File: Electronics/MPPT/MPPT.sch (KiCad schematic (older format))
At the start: 24 parts, among them J1 Solar Array, J2 Battery, J3 Car Power, Q1 NMOS, Q2 NMOS

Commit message: MPPT: Add power lines and regulators
There are three primary power regions on the board: the high power regions around the DC/DC Converter, the car's "low" power regions (+12V), and the low power regions around the Nucleo.

The high power regions include current sensors and FET drivers which require power from the car's low power line rather than the high power lines from the solar array and the battery. We use a 12V-12V DC isolator to provide this safely.

We also isolate power to the Nucleo for safety when attaching a computer to the board. Finally, the CAN lines have an isolated power region, but this is managed by the CAN chip.
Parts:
- added U?: Nucleo_L432KC, symbol Nucleo_L432KC
- added U?: PDS1-S12-S9-M, symbol PDS1-S12-S9-M
- added U?: PDM2-S12-S12-S, symbol PDM2-S12-S12-S
- C3: value CP1 -> CP
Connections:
- net labels added: +12V, +5V, +9V, GND
- wire segments 94 -> 86
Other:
- note added: "High Power\nControl"
- note added: "Isolated Power Regions:\n* High Power\n - Arr+\n - Batt+\n - +12P\n - GNDPWR\n* Low Car Power\n - +12V\n - GNDREF\n* Nucleo/Computer Power\n - +9V\n - +5V\n - GND"
- note added: "Note: Current sensors may be\non ground line, not high line"
- note added: "Nucleo Power"
- note added: "Power Regulation"
- note removed: "Power and Isolation"
- moved on the sheet: J3

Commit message: MPPT: Add FET driver and its Nucleo connection
The FET driver doesn't provide any isolation, and it needs to be on the High Power plane, so we will need to add isolation on its PWM input to protect the Nucleo.

We should also figure out whether tying the chip's Enable pin to the PWM input is appropriate or not. According to the datasheet, the enable pin is internally pulled up to Vdd by a 100Kohm resistor, so it may draw unexpected current from the PWM line.
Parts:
- added R?: 1R5, symbol R
- added U?: UCC27321, symbol UCC27321
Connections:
- wire segments 86 -> 99
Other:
- note added: "TODO: Add isolation here.\nEither a new chip or an isolating\nchip on the Nucleo side."
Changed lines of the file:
@@
 LIBS:utsvt-power-regulators
 LIBS:utsvt-microcontrollers
+LIBS:utsvt-connectors
+LIBS:utsvt-chips
 LIBS:MPPT-cache
 EELAYER 25 0
@@
 Wire Notes Line
 	10400 650  7750 650
+Wire Wire Line
+	6300 4900 7100 4900
+$Comp
+L UCC27321 U?
+U 1 1 5BBC0485
+P 7600 4950
+F 0 "U?" H 7600 4700 60  0000 C CNN
+F 1 "UCC27321" H 7600 5200 60  0000 C CNN
+F 2 "" H 7600 4950 60  0001 C CNN
+F 3 "" H 7600 4950 60  0001 C CNN
+	1    7600 4950
+	1    0    0    -1
+$EndComp
+$Comp
+L R R?
+U 1 1 5BBC08B0
+P 8450 4900
+F 0 "R?" V 8530 4900 50  0000 C CNN
+F 1 "1R5" V 8450 4900 50  0000 C CNN
+F 2 "" V 8380 4900 50  0001 C CNN
+F 3 "" H 8450 4900 50  0001 C CNN
+	1    8450 4900
+	0    1    1    0
+$EndComp
+Wire Wire Line
+	8100 4900 8300 4900
+Wire Wire Line
+	8100 5000 8200 5000
+Wire Wire Line
+	8200 5000 8200 4900
+Connection ~ 8200 4900
+Wire Wire Line
+	8600 4900 8700 4900
+Text Label 8700 4900 0    60   ~ 12
+Drive_PWM
+$Comp
+L +12P #PWR?
+U 1 1 5BBC0ED7
+P 8150 4750
+F 0 "#PWR?" H 8150 4600 50  0001 C CNN
+F 1 "+12P" H 8150 4890 50  0000 C CNN
+F 2 "" H 8150 4750 50  0001 C CNN
+F 3 "" H 8150 4750 50  0001 C CNN
+	1    8150 4750
+	1    0    0    -1
+$EndComp
+$Comp
+L GNDPWR #PWR?
+U 1 1 5BBC0FAD
+P 8150 5150
+F 0 "#PWR?" H 8150 4950 50  0001 C CNN
+F 1 "GNDPWR" H 8150 5020 50  0000 C CNN
+F 2 "" H 8150 5100 50  0001 C CNN
+F 3 "" H 8150 5100 50  0001 C CNN
+	1    8150 5150
+	1    0    0    -1
+$EndComp
+Wire Wire Line
+	8100 5100 8150 5100
+Wire Wire Line
+	8150 5100 8150 5150
+Wire Wire Line
+	8100 4800 8150 4800
+Wire Wire Line
+	8150 4800 8150 4750
+$Comp
+L +12P #PWR?
+U 1 1 5BBC1539
+P 7050 4750
+F 0 "#PWR?" H 7050 4600 50  0001 C CNN
+F 1 "+12P" H 7050 4890 50  0000 C CNN
+F 2 "" H 7050 4750 50  0001 C CNN
+F 3 "" H 7050 4750 50  0001 C CNN
+	1    7050 4750
+	1    0    0    -1
+$EndComp
+Wire Wire Line
+	7050 4750 7050 4800
+Wire Wire Line
+	7050 4800 7100 4800
+$Comp
+L GNDPWR #PWR?
+U 1 1 5BBC165F
+P 7050 5150
+F 0 "#PWR?" H 7050 4950 50  0001 C CNN
+F 1 "GNDPWR" H 7050 5020 50  0000 C CNN
+F 2 "" H 7050 5100 50  0001 C CNN
+F 3 "" H 7050 5100 50  0001 C CNN
+	1    7050 5150
+	1    0    0    -1
+$EndComp
+Wire Wire Line
+	7050 5150 7050 5100
+Wire Wire Line
+	7050 5100 7100 5100
+Text Notes 6950 4450 0    60   ~ 12
+TODO: Add isolation here.\nEither a new chip or an isolating\nchip on the Nucleo side.
 $EndSCHEMATC

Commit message: MPPT: Add current sensors and current/voltage sensor connections to Nucleo
I moved the current sensors from the high-side to the low-side for safety reasons - namely, the common-mode voltage has now dropped from >60V to ~0V. I also renamed the sensors from In/Out to Array/Battery for clarity's sake.

I still need to add isolation between the Nucleo and the sensors and FET driver, since these are in two very different power regimes. I also need to add CAN hardware, since we have changed the design enough that the old CAN breakout I designed is no longer useful.
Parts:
- added C? (x2): 0.1uF, symbol C_Small
- added R? (x2): 10m, symbol R_Small
- added U? (x2): INA213, symbol INA213
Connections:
- net labels added: +Arr, +Batt, -Arr, -Batt, Array_Current, Array_Voltage, Battery_Current, Battery_Voltage
- net labels removed: Array+, Batt+, DC_In+, DC_Out+, Input_Voltage, Output_Voltage
- wire segments 99 -> 137
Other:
- note added: "Array\nCurrent\nSensor"
- note added: "Array\nVoltage\nSensor"
- note added: "Basic voltage\ndividers"
- note added: "Battery\nCurrent\nSensor"
- note added: "Battery\nVoltage\nSensor"
- note added: "GNDPWR"
- note added: "Isolated Power Regions:\n* High Power\n - +/-Arr\n - +/-Batt\n - +12P\n - GNDPWR\n* Low Car Power\n - +12V\n - GNDREF\n* Nucleo/Computer Power\n - +9V\n - +5V\n - GND"
- note added: "Low-side\ncurrent\nsense"
- note added: "Nucleo Connections"
- note added: "TODO: Add isolation to\nall of these inputs"
- note added: "This looks weird,\nbut it is correct.\nCurrent flows out\nof battery's -."
- note added: "This looks weird,\nbut it is correct.\nCurrent flows\ninto array's -."
- note removed: "Input Voltage"
- note removed: "Input\nCurrent\nSensor"
- note removed: "Input\nVoltage\nSensor"
- note removed: "Isolated Power Regions:\n* High Power\n - Arr+\n - Batt+\n - +12P\n - GNDPWR\n* Low Car Power\n - +12V\n - GNDREF\n* Nucleo/Computer Power\n - +9V\n - +5V\n - GND"
- note removed: "Note: Current sensors may be\non ground line, not high line"
- note removed: "Nucleo"
- note removed: "Output Voltage"
- note removed: "Output\nCurrent\nSensor"
- note removed: "Output\nVoltage\nSensor"
- moved on the sheet: D?, F1, J2, R?, U?

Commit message: MPPT: Combine Nucleo and High Power planes; add test points.
Unfortunately, there's not a good way to isolate the Nucleo from the high power plane without redesigning our sensors entirely, and it's too late for that. This means we need to combine their power planes together.
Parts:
- removed U?: PDS1-S12-S9-M, symbol PDS1-S12-S9-M
- added TP1: +ARR, symbol TEST
- added TP10: Batt_I, symbol TEST
- added TP11: PWM, symbol TEST
- added TP12: GATE, symbol TEST
- added TP2: +BATT, symbol TEST
- added TP3: +SNUB, symbol TEST
- added TP4: SNUB_MID, symbol TEST
- added TP5: +12P, symbol TEST
- added TP6: GNDP, symbol TEST
- added TP7: Arr_V, symbol TEST
- added TP8: Batt_V, symbol TEST
- added TP9: Arr_I, symbol TEST
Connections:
- net labels added: Reset
- net labels removed: +9V, GND
- wire segments 137 -> 140
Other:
- note added: "Isolated Power Regions:\n* High Power/Nucleo\n - +/-Arr\n - +/-Batt\n - +12P\n - +9V\n - +5V\n - GNDPWR\n* Low Car Power\n - +12V\n - GNDREF"
- note added: "NOTE: We would ordinarily isolate the Nucleo from\nthe high power regions, but we don't have a good\nway to do that without redesigning our sensors and\nour software. Therefore, for reasons of expediency,\nwe're placing the Nucleo on the high power plane."
- note removed: "Isolated Power Regions:\n* High Power\n - +/-Arr\n - +/-Batt\n - +12P\n - GNDPWR\n* Low Car Power\n - +12V\n - GNDREF\n* Nucleo/Computer Power\n - +9V\n - +5V\n - GND"
- note removed: "Nucleo Power"
- note removed: "TODO: Add isolation here.\nEither a new chip or an isolating\nchip on the Nucleo side."
- note removed: "TODO: Add isolation to\nall of these inputs"
- moved on the sheet: J3, R?, U?

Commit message: MPPT: Add CAN electronics. Change high power control to 9V from 12V.
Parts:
- removed U?: PDM2-S12-S12-S, symbol PDM2-S12-S12-S
- added C10: 0.22u, symbol C_Small
- added C11, C14, C15, C6, C8: 0.1u, symbol C_Small
- added C12, C16: 0.01u, symbol C_Small
- added C13, C9: 10u, symbol C_Small
- added C4, C5: ?F, symbol C_Small
- added C7: 1u, symbol C_Small
- added J4: CAN_In, symbol CANConnector
- added J5: CAN_Out, symbol CANConnector
- added JP1: Termination Resistors, symbol Jumper_NO_Small
- added L2, L3: 2k, symbol Ferrite_Bead_Small
- added R10, R9: 60, symbol R
- added SW1: RESET, symbol SW_Push
- added TP13: CAN_ISO_Vout, symbol TEST
- added TP14: CAN_ISO_Vin, symbol TEST
- added TP15: CAN_ISO_GndIn, symbol TEST
- added TP16: CAN_ISO_GndOut, symbol TEST
- added U1: PDS1-S12-S9-M, symbol PDS1-S12-S9-M
- added U5: ADM3055E, symbol ADM3055E
- TP5: value +12P -> +9VA
- gave numbers to parts that had none: 17
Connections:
- net labels added: +3.3V, +9VA, CAN_Rx, CAN_Tx
- net labels removed: +12P
- wire segments 140 -> 222
- no-connect marks 0 -> 20
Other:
- note added: "CAN"
- note added: "For decoupling, we\nadd extra capacitors\nand unlink the power\npins on either side"
- note added: "Isolated Power Regions:\n* High Power/Nucleo\n - +/-Arr\n - +/-Batt\n - +9A, +5V, +3.3V\n - GNDPWR\n* Low Car Power\n - +12V\n - GNDREF"
- note added: "Must be close\nto V_ISO_In"
- note added: "Must be close\nto V_ISO_Out"
- note added: "This is really complicated.\nI blame Analog Devices."
- note removed: "Isolated Power Regions:\n* High Power/Nucleo\n - +/-Arr\n - +/-Batt\n - +12P\n - +9V\n - +5V\n - GNDPWR\n* Low Car Power\n - +12V\n - GNDREF"
- moved on the sheet: C17, C18, J3, R11, R7, R8, TP10, TP11, TP12, TP5, TP6, TP9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

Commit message: MPPT: Selected footprints for all components*.
Some footprints are approximate placeholders until I can be sure what their footprints really are. Specifically, the following components have placeholder footprints:

* Snubber components
* All connectors
* Current Sense shunt resistors
* Filtering and bypass capacitors surrounding CAN transceiver

Also added datasheet for the inductor we're planning to use.
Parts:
- C1, C2: footprint (none) -> UTSVT_Passive:CP_Radial_D31mm_P9mm
- C10, C11, C12, C13, C14, C15, C16, C9: footprint (none) -> Capacitors_SMD:C_0805
- C17, C18, C5, C6, C8: footprint (none) -> Capacitors_SMD:C_0805_HandSoldering
- C3, C7: footprint (none) -> Capacitors_THT:CP_Radial_D10.0mm_P5.00mm
- C4: value ?F -> 4.7u; footprint (none) -> Capacitors_SMD:C_0805_HandSoldering
- D1: footprint (none) -> Diodes_THT:D_5W_P10.16mm_Horizontal
- D2, D3: footprint (none) -> TO_SOT_Packages_THT:TO-220-2_Vertical
- D4: footprint (none) -> Diodes_SMD:D_SMA_Handsoldering
- D5, D7: footprint (none) -> Diodes_SMD:D_SOD-123F
- D6, D8: footprint (none) -> Diodes_SMD:D_SOD-123
- F1: footprint (none) -> Fuse_Holders_and_Fuses:Fuseholder5x20_horiz_open_inline_Type-I
- J1, J2: footprint (none) -> Connectors_Molex:Molex_Mini-Fit_Sr_42820-22XX_1x02_Pitch10.00mm_Horizontal
- J3: footprint (none) -> Connectors_Molex:Molex_MiniFit-JR-5556-02A_2x01x4.20mm_Straight
- J4, J5: footprint (none) -> Connectors_Molex:Molex_NanoFit_1x04x2.50mm_Angled
- JP1: footprint (none) -> Pin_Headers:Pin_Header_Straight_1x02_Pitch2.54mm
- L1: value Ferrite 560uH -> 560uH; footprint (none) -> Inductors_THT:L_Toroid_Vertical_L46.0mm_W19.1mm_P21.80mm_Bourns_5700
- L2, L3: footprint (none) -> Inductors_SMD:L_0805
- Q1, Q2: value NMOS -> 200N25N; footprint (none) -> TO_SOT_Packages_THT:TO-220-3_Vertical
- R1: footprint (none) -> Resistors_THT:R_Axial_Power_L20.0mm_W6.4mm_P22.40mm
- R10, R2, R3, R4, R5, R6, R7, R9: footprint (none) -> Resistors_SMD:R_1206_HandSoldering
- R11, R8: footprint (none) -> Resistors_SMD:R_2816_HandSoldering
- SW1: footprint (none) -> Buttons_Switches_THT:SW_PUSH_6mm
- TP1, TP10, TP11, TP12, TP13, TP14, TP15, TP16, TP2, TP3, TP4, TP5, TP6, TP7, TP8, TP9: footprint (none) -> Measurement_Points:Test_Point_Keystone_5005-5009_Compact
- U1: footprint (none) -> UTSVT_ICs:PDS1-M
- U2: footprint (none) -> UTSVT_Special:NucleoL432KC
- U3: value UCC27321 -> UCC37321; footprint (none) -> UTSVT_ICs:SOIC-8_4.00x5.00mm_Pitch1.27mm; symbol UCC27321 -> UCC37321
- U4, U6: footprint (none) -> UTSVT_ICs:SOIC-6_1.40x2.15mm_Pitch0.65mm; symbol INA213 -> INA21x
- U5: footprint (none) -> UTSVT_ICs:SOIC-20W_7.5x15.4mm_Pitch1.27mm
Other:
- moved on the sheet: C6, C7, C8, R7, TP12, U3

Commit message: MPPT: Update connector components and footprints.
I've made custom schematic symbols for our connectors, since they're supposed to be standardized across the vehicle. The battery and the array both use right-angle variants of the Phoenix Connectors Power Combicon 5 connector, while the low power bus and CAN bus both use vertical variants of the Molex MicroFit 3.0 connector.
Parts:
- J1: footprint Connectors_Molex:Molex_Mini-Fit_Sr_42820-22XX_1x02_Pitch10.00mm_Horizontal -> UTSVT_Connectors:PhoenixContact_PowerCombicon5_GF_3x7.62mm; symbol Conn_01x02 -> SolarArrayConnector
- J2: footprint Connectors_Molex:Molex_Mini-Fit_Sr_42820-22XX_1x02_Pitch10.00mm_Horizontal -> UTSVT_Connectors:PhoenixContact_PowerCombicon5_GF_2x7.62mm; symbol Conn_01x02 -> BatteryConnector
- J3: footprint Connectors_Molex:Molex_MiniFit-JR-5556-02A_2x01x4.20mm_Straight -> UTSVT_Connectors:Molex_MicroFit3.0_1x3xP3.00mm_PolarizingPeg_Vertical; symbol Conn_01x02 -> CarPowerConnector
- J4, J5: footprint Connectors_Molex:Molex_NanoFit_1x04x2.50mm_Angled -> UTSVT_Connectors:Molex_MicroFit3.0_1x4xP3.00mm_PolarizingPeg_Vertical
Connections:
- net +12V: now also J3.1 (+12V); no longer J3.2 (Pin_2)
- net +Arr: now also J1.1 (+); no longer J1.2 (Pin_2)
- net -Arr: now also J1.3 (-); no longer J1.1 (Pin_1)
- net -Batt: now also J2.2 (-); no longer J2.1 (Pin_1)
- net GNDREF: now also J3.3 (GND); no longer J3.1 (Pin_1)
- net at F1.1: now also J2.1 (+); no longer J2.2 (Pin_2)
- no-connect marks 20 -> 21
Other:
- moved on the sheet: J2

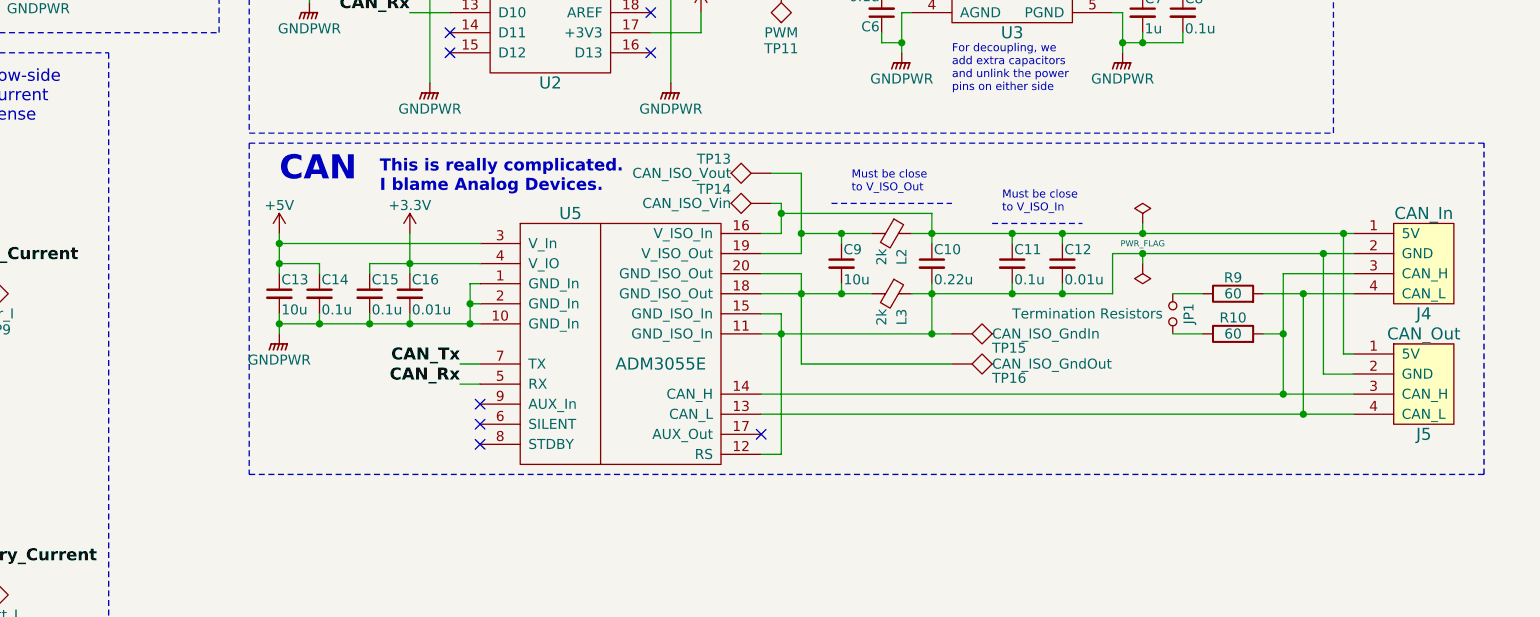
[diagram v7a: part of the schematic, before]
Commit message: MPPT: Insert CAN bus protector into CAN circuit.
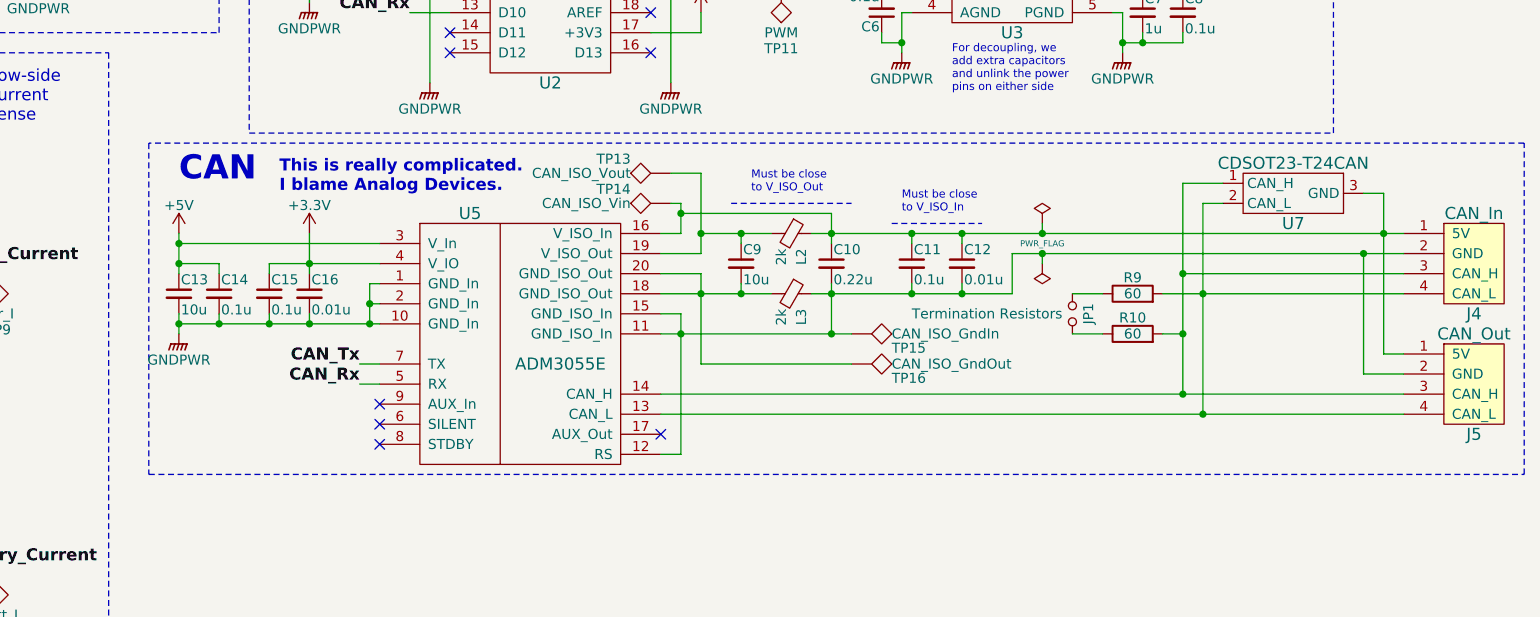
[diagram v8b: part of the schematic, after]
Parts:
- added U7: CDSOT23-T24CAN, TO_SOT_Packages_SMD:SOT-23W, symbol CDSOT23-T24CAN
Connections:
- net at C10.1, C11.1, C12.1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: now also U7.3 (GND)
- net at J4.3 (CAN_H), J5.3 (CAN_H), R10.2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: now also U7.1 (CAN_H)
- net at J4.4 (CAN_L), J5.4 (CAN_L), R9.2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: now also U7.2 (CAN_L)
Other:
- moved on the sheet: C10, C11, C12, C13, C14, C15, C16, C9, J4, J5, JP1, L2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
